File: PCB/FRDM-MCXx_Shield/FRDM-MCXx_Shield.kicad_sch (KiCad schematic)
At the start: 2 parts, among them IC3 M95010-RMN6TP

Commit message: Updated schematic
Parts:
- removed IC3: M95010-RMN6TP, SOIC127P600X175-8N, symbol SamacSys_Parts:M95010-RMN6TP
- added C7: 100nF, Capacitor_SMD:C_0603_1608Metric_Pad1.08x0.95mm_HandSolder, symbol Device:C
- added RN2: 4.7k, Resistor_SMD:R_Array_Convex_4x0603, symbol Device:R_Pack04_Split
- added U3: M95010-RMN6TP, SOIC127P600X175-8N, symbol SamacSys_Parts:M95010-RMN6TP
- J2: footprint (none) -> User:MCX-A153_Shield_Template
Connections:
- new net +3.3V: C7.1, RN2.5 (R4.2), RN2.6 (R3.2), U3.3 (~{W}), U3.8 (VCC)
- new net GND: C7.2, U3.4 (VSS)
- new net SCL: RN2.3 (R3.1)
- new net SDA: RN2.4 (R4.1)
- new net SPI_CLK: U3.6 (C)
- new net SPI_MISO: U3.2 (Q)
- new net SPI_MOSI: U3.5 (D)
- new net ~{EEPROM_CS}: U3.1 (~{S})
- no-connect marks 0 -> 1
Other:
- sheet Actuators ports: added LED_NEOPIXEL, SERVO_PWM, SPI_CLK, SPI_MISO, SPI_MOSI, ~{SPI_CS}; removed none
- sheet HMI ports: added ENC_A, ENC_B, ENC_SW, LED_B, LED_G, LED_R, SCL, SDA, SWITCH; removed none
- sheet Sensors ports: added ACEL_CS, ACEL_INT1, ACEL_INT2, ADC_OUT, GPS_PPS, GPS_RX, GPS_TX, SCL, SDA, SPI_CLK, SPI_MISO, SPI_MOSI, TEMP_ALERT, ~{TEMP_RST}; removed none
- company: (none) -> HAN
- title: (none) -> Main

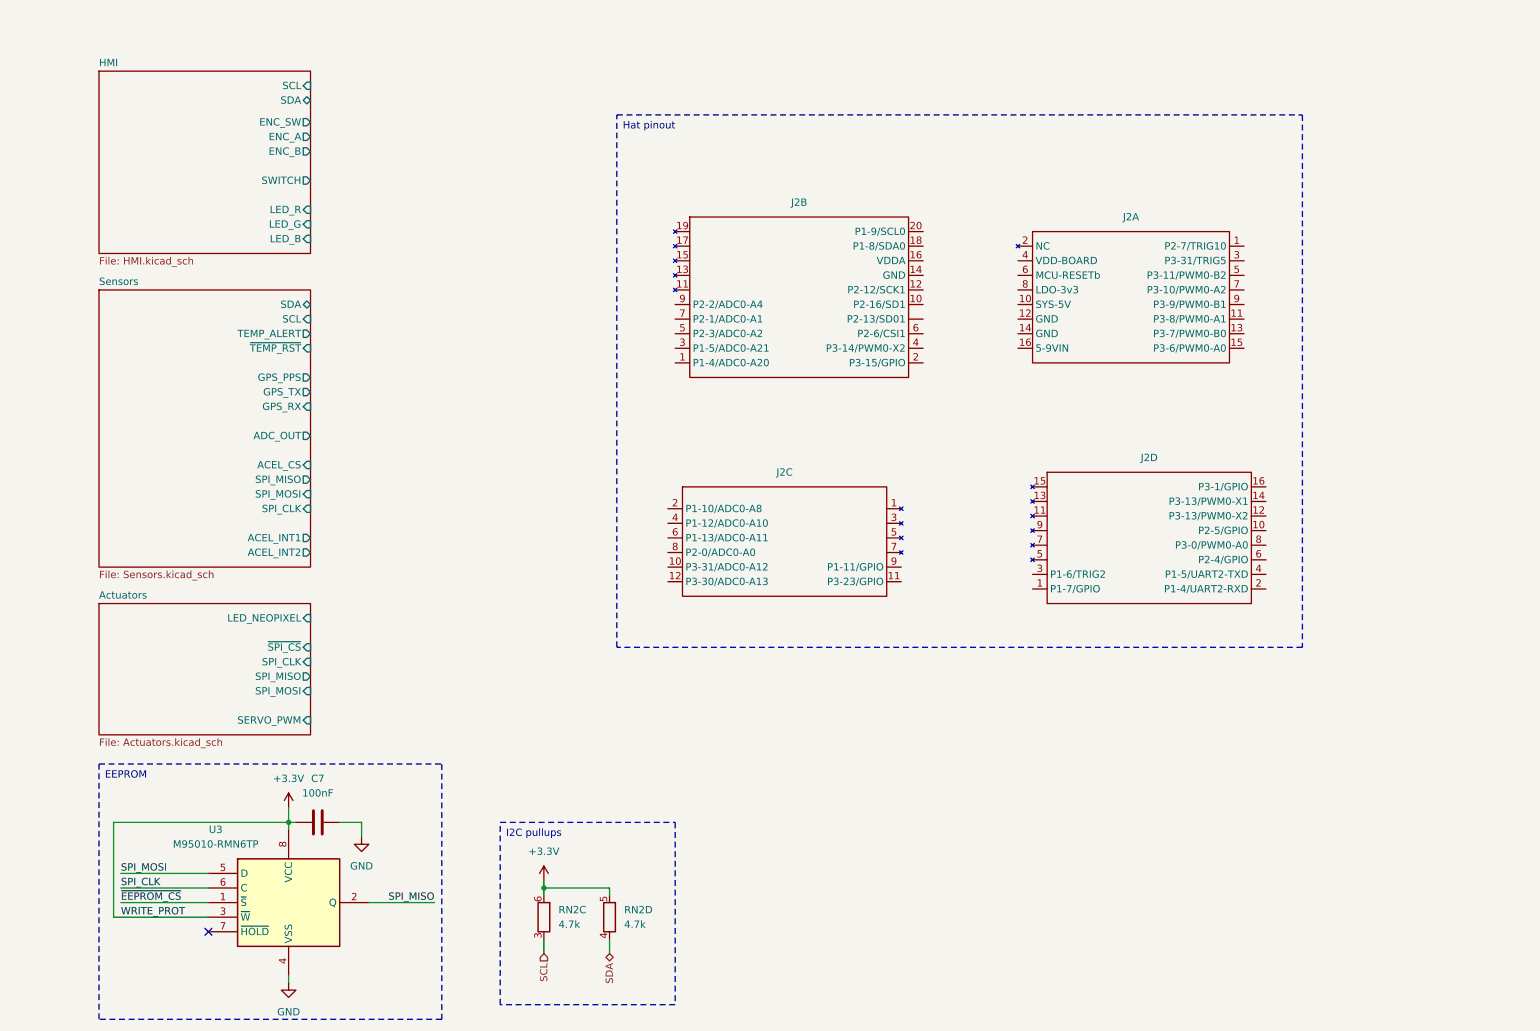
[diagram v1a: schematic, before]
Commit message: Update schematic and footprint
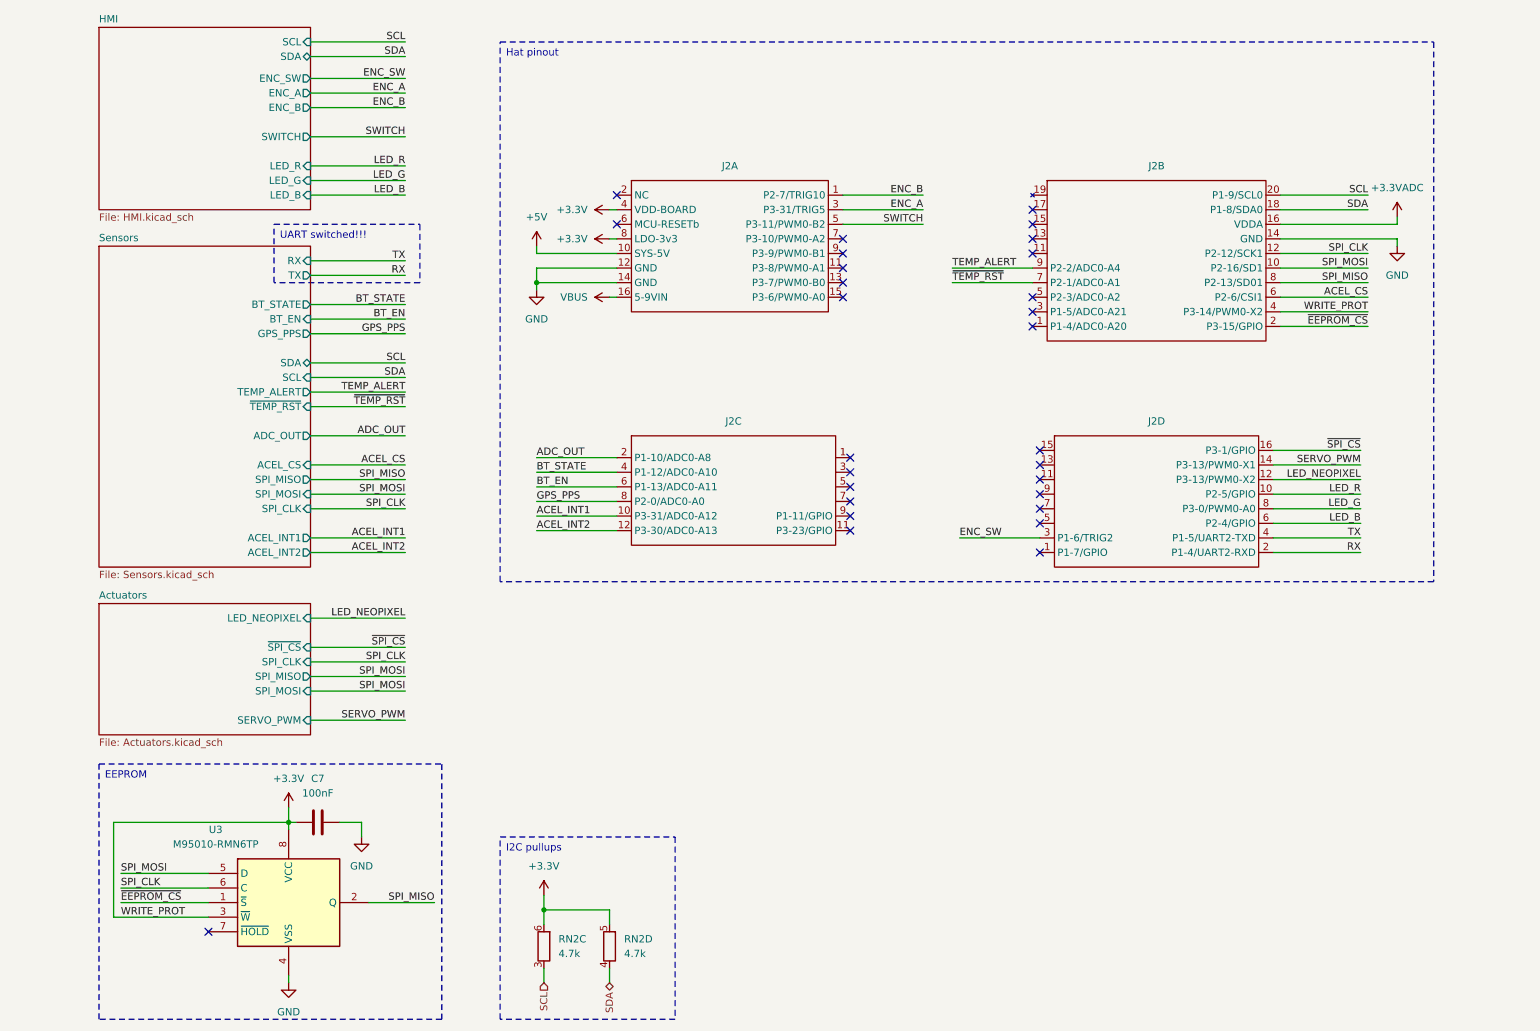
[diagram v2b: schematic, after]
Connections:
- net +3.3V: now also J2.4 (P3-14/PWM0-X2), J2.4 (VDD-BOARD), J2.8 (LDO-3v3)
- net GND: now also J2.12 (GND), J2.14 (GND), J2.14 (GND)
- net SCL: now also J2.20 (P1-9/SCL0)
- net SDA: now also J2.18 (P1-8/SDA0)
- net SPI_CLK: now also J2.12 (P2-12/SCK1)
- net SPI_MISO: now also J2.8 (P2-13/SD01)
- net SPI_MOSI: now also J2.10 (P2-16/SD1)
- net ~{EEPROM_CS}: now also J2.2 (P3-15/GPIO)
- net +3.3VADC: now reaches J2.16 (VDDA)
- net ACEL_CS: now reaches J2.6 (P2-6/CSI1)
- net ~{TEMP_RST}: now reaches J2.7 (P2-1/ADC0-A1)
- net TEMP_ALERT: now reaches J2.9 (P2-2/ADC0-A4)
- net ACEL_INT1: now reaches J2.10 (P3-31/ADC0-A12)
- net ACEL_INT2: now reaches J2.12 (P3-30/ADC0-A13)
- net ADC_OUT: now reaches J2.2 (P1-10/ADC0-A8)
- net BT_STATE: now reaches J2.4 (P1-12/ADC0-A10)
- net BT_EN: now reaches J2.6 (P1-13/ADC0-A11)
- net GPS_PPS: now reaches J2.8 (P2-0/ADC0-A0)
- net ENC_B: now reaches J2.1 (P2-7/TRIG10)
- net +5V: now reaches J2.10 (SYS-5V)
- net VBUS: now reaches J2.16 (5-9VIN)
- net ENC_A: now reaches J2.3 (P3-31/TRIG5)
- net SWITCH: now reaches J2.5 (P3-11/PWM0-B2)
- net LED_R: now reaches J2.10 (P2-5/GPIO)
- net LED_NEOPIXEL: now reaches J2.12 (P3-13/PWM0-X2)
- net SERVO_PWM: now reaches J2.14 (P3-13/PWM0-X1)
- net ~{SPI_CS}: now reaches J2.16 (P3-1/GPIO)
- net RX: now reaches J2.2 (P1-4/UART2-RXD)
- net ENC_SW: now reaches J2.3 (P1-6/TRIG2)
- net TX: now reaches J2.4 (P1-5/UART2-TXD)
- net LED_B: now reaches J2.6 (P2-4/GPIO)
- net LED_G: now reaches J2.8 (P3-0/PWM0-A0)
- no-connect marks 1 -> 28
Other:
- sheet Sensors ports: added BT_EN, BT_STATE, RX, TX; removed GPS_RX, GPS_TX
- moved on the sheet: RN2C, RN2D

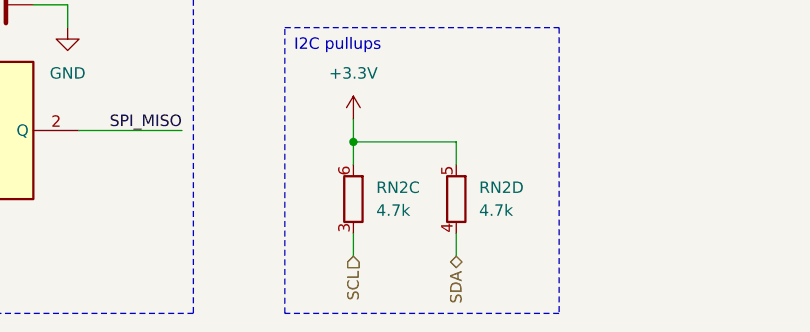
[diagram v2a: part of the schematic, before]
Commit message: Updated schematic and PCB
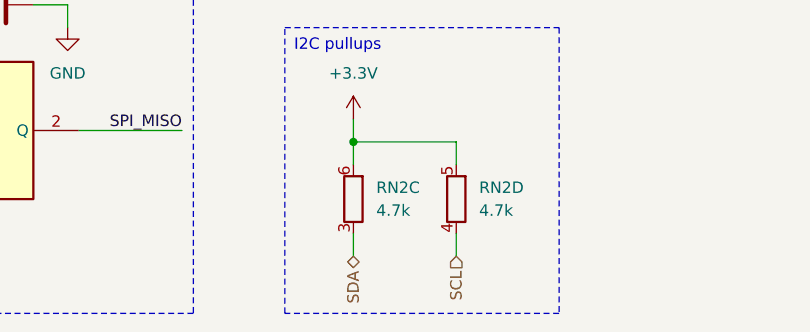
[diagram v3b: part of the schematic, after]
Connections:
- net SCL: now also RN2.4 (R4.1); no longer RN2.3 (R3.1)
- net SDA: now also RN2.3 (R3.1); no longer RN2.4 (R4.1)
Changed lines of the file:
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@@
     (effects (font (size 1.27 1.27)) (justify right bottom))
   )
-  (hierarchical_label "SDA" (shape bidirectional) (at 118.11 186.69 270) (fields_autoplaced)
+  (hierarchical_label "SDA" (shape bidirectional) (at 106.68 186.69 270) (fields_autoplaced)
     (effects (font (size 1.27 1.27)) (justify right))
   )
-  (hierarchical_label "SCL" (shape input) (at 106.68 186.69 270) (fields_autoplaced)
+  (hierarchical_label "SCL" (shape input) (at 118.11 186.69 270) (fields_autoplaced)
     (effects (font (size 1.27 1.27)) (justify right))
   )

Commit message: Updated schematic and PCB files
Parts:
- added D1: RED, LED_SMD:LED_0603_1608Metric_Pad1.05x0.95mm_HandSolder, symbol Device:LED
- added D2: GREEN, LED_SMD:LED_0603_1608Metric_Pad1.05x0.95mm_HandSolder, symbol Device:LED
- added D3: BZV55B9V1, Diode_SMD:D_SOD-128, symbol Diode:BZV55B9V1
- added F1: 300mA, Fuse:Fuse_0603_1608Metric_Pad1.05x0.95mm_HandSolder, symbol Device:Polyfuse
- added H1: MountingHole, MountingHole:MountingHole_2.5mm, symbol Mechanical:MountingHole
- added J2: Barrel_Jack_Switch, BarrelJack_Wuerth_6941xx301002, symbol Connector:Barrel_Jack_Switch
- added Q1: IRLML6401, Package_TO_SOT_SMD:SOT-23, symbol Transistor_FET:IRLML6401
- added R2: 470, Resistor_SMD:R_0603_1608Metric_Pad0.98x0.95mm_HandSolder, symbol Device:R
- added R2: 330, Resistor_SMD:R_0603_1608Metric_Pad0.98x0.95mm_HandSolder, symbol Device:R
- added R2: 100k, Resistor_SMD:R_0603_1608Metric_Pad0.98x0.95mm_HandSolder, symbol Device:R
- renumbered J2 to J1, U3 to U1
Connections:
- net +3.3V: now also J1.A4 (VDD-BOARD), J1.A8 (LDO-3v3), J1.B4 (P3-14/PWM0-X2), R2.1; no longer J1.4 (P3-14/PWM0-X2), J1.4 (VDD-BOARD), J1.8 (LDO-3v3)
- net +3.3VADC: now also J1.B16 (VDDA); no longer J1.16 (VDDA)
- net +5V: now also J1.A10 (SYS-5V), R2.1; no longer J1.10 (SYS-5V)
- net ACEL_CS: now also J1.B6 (P2-6/CSI1); no longer J1.6 (P2-6/CSI1)
- net ACEL_INT1: now also J1.C10 (P3-31/ADC0-A12); no longer J1.10 (P3-31/ADC0-A12)
- net ACEL_INT2: now also J1.C12 (P3-30/ADC0-A13); no longer J1.12 (P3-30/ADC0-A13)
- net ADC_OUT: now also J1.C2 (P1-10/ADC0-A8); no longer J1.2 (P1-10/ADC0-A8)
- net BT_EN: now also J1.C6 (P1-13/ADC0-A11); no longer J1.6 (P1-13/ADC0-A11)
- net BT_STATE: now also J1.C4 (P1-12/ADC0-A10); no longer J1.4 (P1-12/ADC0-A10)
- net ENC_A: now also J1.A3 (P3-31/TRIG5); no longer J1.3 (P3-31/TRIG5)
- net ENC_B: now also J1.A1 (P2-7/TRIG10); no longer J1.1 (P2-7/TRIG10)
- net ENC_SW: now also J1.D3 (P1-6/TRIG2); no longer J1.3 (P1-6/TRIG2)
- net GND: now also J1.A12 (GND), J1.A14 (GND), J1.B14 (GND), D1.1 (K), D2.1 (K), J2.2, J2.3, R2.2; no longer J1.12 (GND), J1.14 (GND), J1.14 (GND)
- net GPS_PPS: now also J1.C8 (P2-0/ADC0-A0); no longer J1.8 (P2-0/ADC0-A0)
- net LED_B: now also J1.D10 (P2-5/GPIO); no longer J1.6 (P2-4/GPIO)
- net LED_G: now also J1.D8 (P3-0/PWM0-A0); no longer J1.8 (P3-0/PWM0-A0)
- net LED_NEOPIXEL: now also J1.D12 (P3-13/PWM0-X2); no longer J1.12 (P3-13/PWM0-X2)
- net LED_R: now also J1.D6 (P2-4/GPIO); no longer J1.10 (P2-5/GPIO)
- net RX: now also J1.D2 (P1-4/UART2-RXD); no longer J1.2 (P1-4/UART2-RXD)
- net SCL: now also J1.B20 (P1-9/SCL0); no longer J1.20 (P1-9/SCL0)
- net SDA: now also J1.B18 (P1-8/SDA0); no longer J1.18 (P1-8/SDA0)
- net SERVO_PWM: now also J1.D14 (P3-13/PWM0-X1); no longer J1.14 (P3-13/PWM0-X1)
- net SPI_CLK: now also J1.B12 (P2-12/SCK1); no longer J1.12 (P2-12/SCK1)
- net SPI_MISO: now also J1.B8 (P2-13/SD01); no longer J1.8 (P2-13/SD01)
- net SPI_MOSI: now also J1.B10 (P2-16/SD1); no longer J1.10 (P2-16/SD1)
- net SWITCH: now also J1.A5 (P3-11/PWM0-B2); no longer J1.5 (P3-11/PWM0-B2)
- net TEMP_ALERT: now also J1.B7 (P2-1/ADC0-A1); no longer J1.9 (P2-2/ADC0-A4)
- net TX: now also J1.D4 (P1-5/UART2-TXD); no longer J1.4 (P1-5/UART2-TXD)
- net VBUS: now also J1.A16 (5-9VIN), D3.1 (K), Q1.2 (S); no longer J1.16 (5-9VIN)
- net ~{EEPROM_CS}: now also J1.B2 (P3-15/GPIO); no longer J1.2 (P3-15/GPIO)
- net ~{SPI_CS}: now also J1.D16 (P3-1/GPIO); no longer J1.16 (P3-1/GPIO)
- net ~{TEMP_RST}: now also J1.B9 (P2-2/ADC0-A4); no longer J1.7 (P2-1/ADC0-A1)
- new net: D3.2 (A), Q1.1 (G), R2.1
- new net: D2.2 (A), R2.2
- new net: F1.1, J2.1
- new net: F1.2, Q1.3 (D)
- new net: D1.2 (A), R2.2
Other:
- moved on the sheet: C7, J1A, J1B, J1C, J1D, RN2C, RN2D, U1

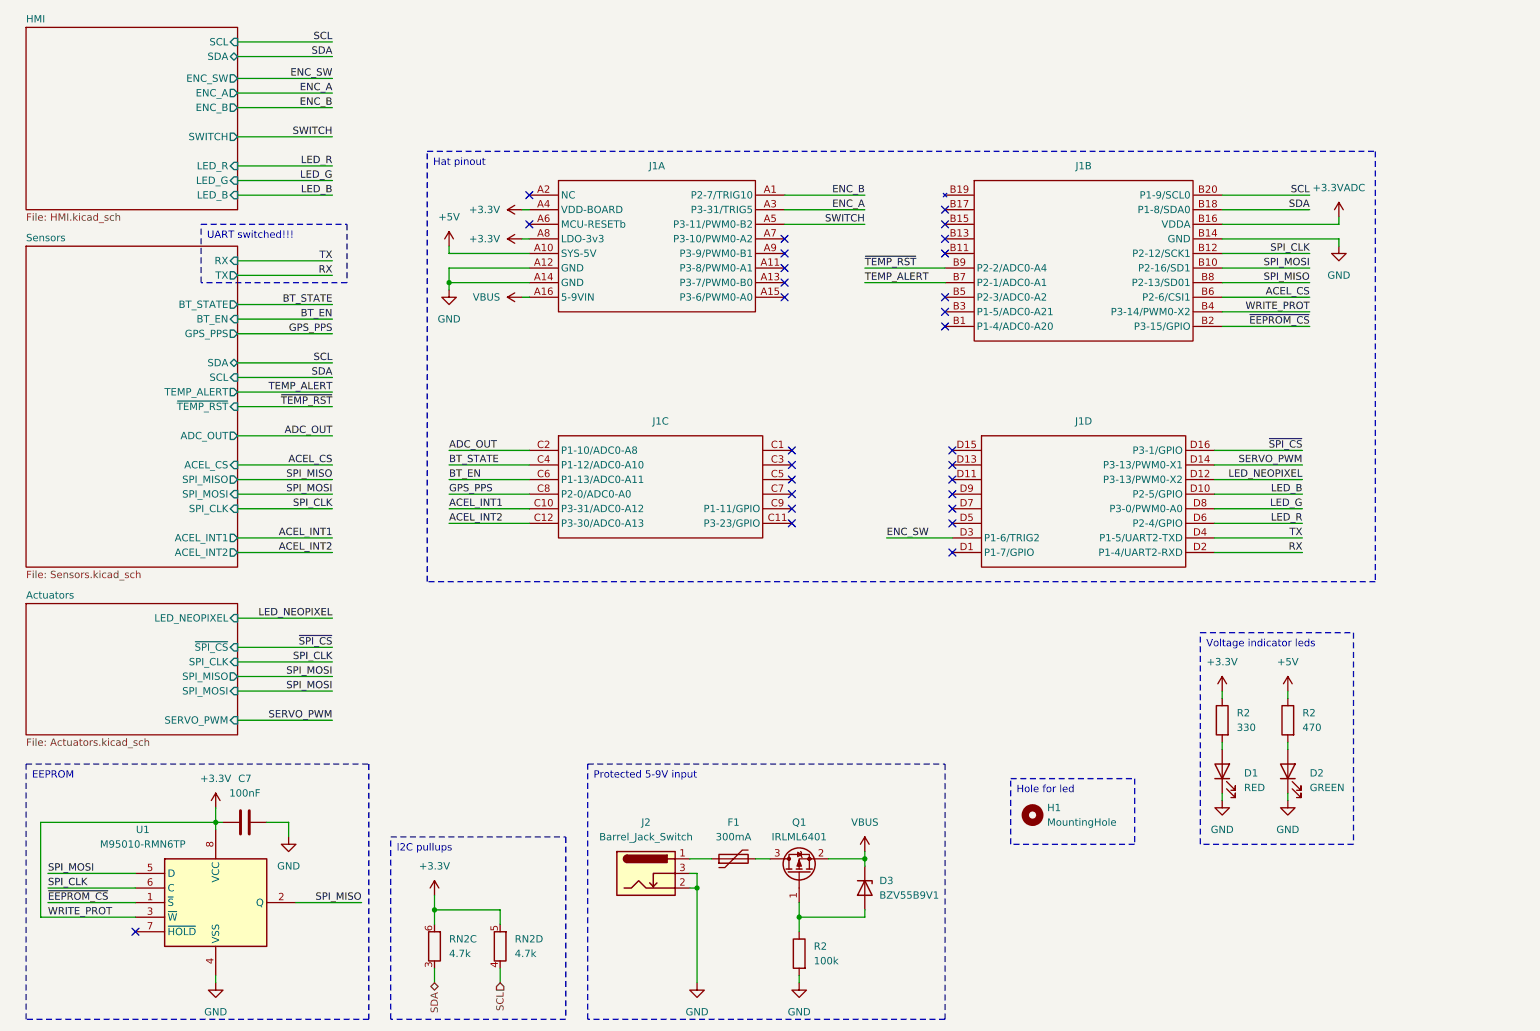
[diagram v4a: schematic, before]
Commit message: Updated schematic and PCB
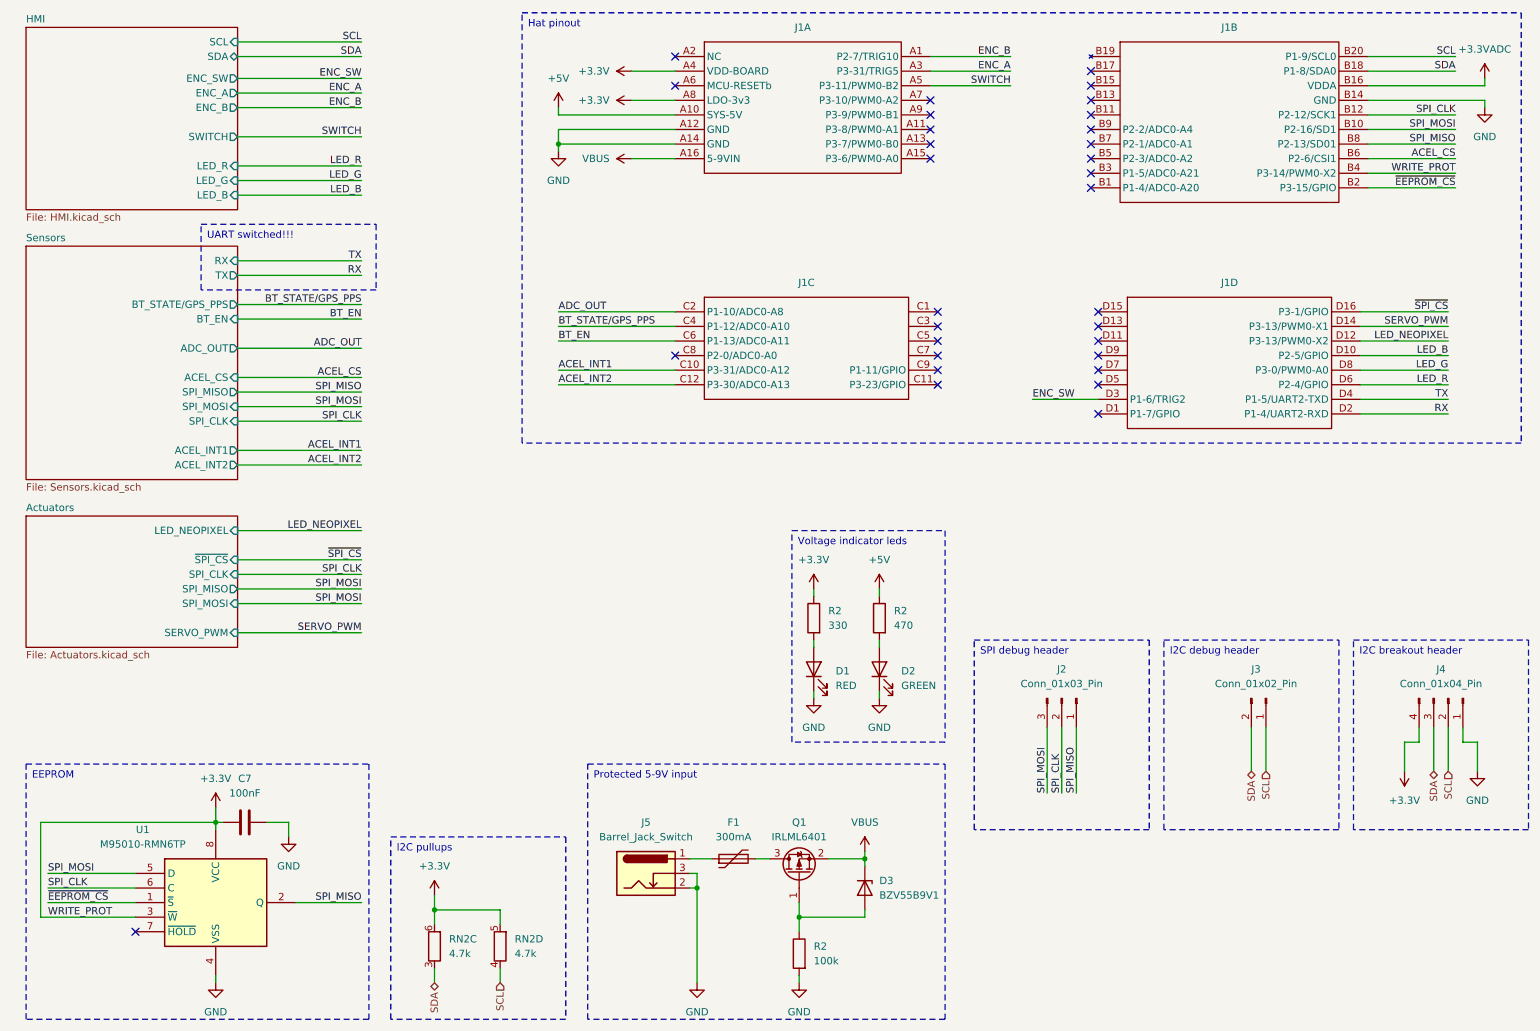
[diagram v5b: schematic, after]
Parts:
- removed H1: MountingHole, MountingHole:MountingHole_2.5mm, symbol Mechanical:MountingHole
- added J2: Conn_01x03_Pin, Connector_PinHeader_2.54mm:PinHeader_1x03_P2.54mm_Vertical, symbol Connector:Conn_01x03_Pin
- added J3: Conn_01x02_Pin, Connector_PinHeader_2.54mm:PinHeader_1x02_P2.54mm_Vertical, symbol Connector:Conn_01x02_Pin
- added J4: Conn_01x04_Pin, Connector_PinHeader_2.54mm:PinHeader_1x04_P2.54mm_Vertical, symbol Connector:Conn_01x04_Pin
- F1: footprint Fuse:Fuse_0603_1608Metric_Pad1.05x0.95mm_HandSolder -> Fuse:Fuse_1206_3216Metric_Pad1.42x1.75mm_HandSolder
- renumbered J2 to J5
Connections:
- net +3.3V: now also J4.4 (Pin_4)
- net GND: now also J4.1 (Pin_1)
- net SCL: now also J3.1 (Pin_1), J4.2 (Pin_2)
- net SDA: now also J3.2 (Pin_2), J4.3 (Pin_3)
- net SPI_CLK: now also J2.2 (Pin_2)
- net SPI_MISO: now also J2.1 (Pin_1)
- net SPI_MOSI: now also J2.3 (Pin_3)
- net BT_STATE renamed BT_STATE/GPS_PPS
- net GPS_PPS: no longer names the net of J1.C8 (P2-0/ADC0-A0)
- net TEMP_ALERT: no longer names the net of J1.B7 (P2-1/ADC0-A1)
- net ~{TEMP_RST}: no longer names the net of J1.B9 (P2-2/ADC0-A4)
- no-connect marks 28 -> 31
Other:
- sheet Sensors ports: added BT_STATE/GPS_PPS; removed BT_STATE, GPS_PPS, SCL, SDA, TEMP_ALERT, ~{TEMP_RST}
- moved on the sheet: D1, D2, J1A, J1B, J1C, J1D, R2
